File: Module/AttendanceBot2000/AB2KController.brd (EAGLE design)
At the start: 107.6 x 80 mm, 51 parts, among them IC1 74AHCT1G04DBV, IC2 74AHCT1G04DBV, IC3 LM386M-1, U1 L298, U2 QRE1113, U3 QRE1113, U4 QRE1113, U5 QRE1113, U6 QRE1113

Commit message: More progress on routing
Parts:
- added JP11: GO_LIGHT, SparkFun-Connectors:SCREWTERMINAL-5MM-2
- added Q1, Q2, Q3, Q4, Q5, Q6: 2N3904, transistor-npn:TO92
- added R11, R12, R13, R14, R15, R16: 1K, resistor:M1206
- moved JP4 37.5 mm to (39.4, 6.35), turned to 0 degrees
- moved JP9 29.5 mm to (38.1, 14.0)
- moved D1 24.7 mm to (33.0, 8.89)
- moved IC2 17.8 mm to (29.2, 24.1), turned to 270 degrees
- moved U$1 15.5 mm to (44.5, 35.6), turned to 180 degrees
- moved JP5 15.5 mm to (5.08, 20.3), turned to 270 degrees
- moved IC1 13.7 mm to (29.2, 17.8), turned to 270 degrees
- moved R7 10.8 mm to (81.3, 68.6), turned to 270 degrees
- moved JP10 7.18 mm to (52.1, 7.62), turned to 270 degrees
- moved R9 6.84 mm to (97.8, 63.5), turned to 270 degrees
- moved U1 5.08 mm to (20.3, 24.1)
- moved R10 2.54 mm to (88.9, 68.6)
- moved R8 2.54 mm to (71.1, 68.6)
- moved JP8 1.80 mm to (5.08, 48.3)
- moved JP6 1.27 mm to (5.08, 34.3)
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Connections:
- new net GO_IN: JP8.1, U$1.13
- new net GO_LT_ON: R16.2, U$1.12
- new net N$10: Q2.3, R3.2
- new net N$12: Q3.3, R5.2
- new net N$15: Q1.2, R11.1
- new net N$17: Q2.2, R12.1
- new net N$24: Q3.2, R13.1
- new net N$26: Q4.2, R14.1
- new net N$29: Q5.2, R15.1
- new net N$30: Q4.3, R7.2
- new net N$31: Q5.3, R9.2
- new net N$6: JP11.1, Q6.1
- new net N$9: Q1.3, R1.2
- net GND: now also Q6.3
- net N$25: now also Q6.2, R16.1; no longer JP8.1, U$1.5
- net SEN_0: now also U$1.18; no longer U$1.17
- net SEN_1: now also U$1.17; no longer U$1.18
- net VCC: now also R11.2, R12.2, R13.2, R14.2, R15.2; no longer R1.2, R3.2, R5.2, R7.2, R9.2
- net V_IN: now also JP11.2, Q1.1, Q2.1, Q3.1, Q4.1, Q5.1
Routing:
- net V_IN: track 0.00 -> 148.9 mm, vias 0 -> 1
- net VCC: track 0.00 -> 133.5 mm
- net GND: track 39.4 -> 98.8 mm
- net N$3: track 0.00 -> 28.6 mm
- net N$2: track 0.00 -> 22.0 mm
- net SEN_0: track 20.7 -> 0.00 mm, vias 1 -> 0
- net SEN_2: track 0.00 -> 18.2 mm, vias 0 -> 1
- net N$14: track 0.00 -> 16.4 mm
- net SEN_3: track 0.00 -> 15.6 mm, vias 0 -> 1
- net SEN_4: track 0.00 -> 15.5 mm, vias 0 -> 1
- net N$1: track 0.00 -> 14.6 mm
- net N$4: track 0.00 -> 13.6 mm
- net N$13: track 0.00 -> 12.1 mm
- net N$11: track 0.00 -> 12.1 mm
- net N$9: track 0.00 -> 11.3 mm
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- added copper zone on layer 16, net GND
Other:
- board size 107.6 x 80 mm -> 101.3 x 80 mm

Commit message: More layout complete
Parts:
- removed C4, C5: 0.15, resistor:C1206K
- removed C6, C7: 10, resistor:D/7343-31W
- removed JP9: FTDI Basic Prog. Port, SparkFun-Connectors:1X06
- moved C2 78.3 mm to (38.1, 66.0), turned to 90 degrees
- moved R16 74.5 mm to (29.2, 50.8), turned to 90 degrees
- moved JP11 58.5 mm to (5.08, 48.3), turned to 270 degrees
- moved Q6 58.0 mm to (22.9, 49.5), turned to 270 degrees
- moved C1 56.9 mm to (63.5, 66.0), turned to 90 degrees
- moved JP10 39.4 mm to (62.2, 45.7), turned to 0 degrees
- moved C3 26.2 mm to (67.3, 11.4), turned to 90 degrees
- moved C10 25.0 mm to (86.4, 38.1), turned to 90 degrees
- moved C8 15.3 mm to (95.2, 25.4), turned to 90 degrees
- moved R22 14.0 mm to (85.1, 6.35)
- moved C9 13.7 mm to (94.0, 16.5), turned to 180 degrees
- moved R23 11.7 mm to (87.6, 12.7)
- moved IC3 11.4 mm to (87.6, 26.7)
- moved JP8 10.2 mm to (15.2, 48.3)
- moved R21 8.98 mm to (87.6, 16.5)
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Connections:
- removed net DTR: JP9.1, U$1.GRN
- net GND: no longer C4.2, C5.2, C6.-, C7.-, JP9.5, JP9.6, U$1.BLK, U$1.GND
- net RXD_TTL: no longer JP9.3, U$1.RXI
- net SEN_3: now also U$1.A6; no longer U$1.20
- net SEN_4: now also U$1.A7; no longer U$1.A4
- net TXD_TTL: no longer JP9.2, U$1.TXO
- net VCC: no longer C4.1, C5.1, C6.+, C7.+, JP9.4, U$1.VCC
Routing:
- net GND: track 98.8 -> 196.1 mm, vias 0 -> 3
- net SEN_0: track 0.00 -> 79.0 mm, vias 0 -> 1
- net SEN_4: track 15.5 -> 86.8 mm, vias 1 -> 2
- net V_IN: track 148.9 -> 212.7 mm, vias 1 -> 7
- net AUDIO_RESET: track 0.00 -> 55.9 mm, vias 0 -> 2
- net DIRB_H: track 0.00 -> 51.9 mm, vias 0 -> 1
- net SEN_3: track 15.6 -> 66.5 mm, vias 1 -> 2
- net VCC: track 133.5 -> 181.8 mm
- net N$27: track 0.00 -> 46.8 mm
- net SEN_1: track 15.7 -> 58.1 mm
- net DIRA_H: track 0.00 -> 38.6 mm
- net SEN_2: track 18.2 -> 55.4 mm
- net R_PWM: track 0.00 -> 33.5 mm
- net DIRB_L: track 0.00 -> 32.9 mm, vias 0 -> 1
- net AUD_TXD: track 0.00 -> 27.9 mm
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- removed copper zone on layer 16, net GND

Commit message: Finished routing.  Sleep on it for a day
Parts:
- removed FRAME2: FRAME-LETTER, SparkFun-Aesthetics:CREATIVE_COMMONS
- added JP9: SERIAL, SparkFun-Connectors:1X03
- JP3: value L_MOT -> SPKR
- moved JP3 26.7 mm to (66.0, 6.35)
- moved C3 2.54 mm to (67.3, 14.0)
- moved JP1 2.54 mm to (61.0, 38.1)
- moved JP2 2.54 mm to (81.3, 38.1)
- moved JP7 2.54 mm to (66.0, 29.2)
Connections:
- net GND: now also JP9.2
- net RXD_TTL: now also JP9.1
- net TXD_TTL: now also JP9.3
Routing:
- net L_PWM: track 0.00 -> 79.9 mm, vias 0 -> 1
- net GND: track 196.1 -> 250.9 mm, vias 3 -> 6
- net V_IN: track 212.7 -> 245.7 mm, vias 7 -> 8
- net N$19: track 27.3 -> 60.3 mm
- net RXD_TTL: track 0.00 -> 26.7 mm
- net DIRA_L: track 0.00 -> 15.7 mm, vias 0 -> 1
- net TXD_TTL: track 0.00 -> 14.0 mm
- net DIRA_H: track 38.6 -> 50.0 mm
- net DIRB_H: track 51.9 -> 60.8 mm, vias 1 -> 2
- net AUDIO_RESET: track 55.9 -> 61.0 mm
- net VCC: track 181.8 -> 184.3 mm, vias 0 -> 2
- net SEN_0: track 79.0 -> 76.5 mm
- net N$27: track 46.8 -> 49.4 mm
- net AUD_TXD: track 27.9 -> 25.4 mm
- net AUD_RXD: track 27.9 -> 25.4 mm
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- added copper zone on layer 16, net GND
- added copper zone on layer 1, net VCC
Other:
- board text added: "+ -"
- board text added: "AUDIO"
- board text added: "AttBot2K (C) M. H. Reilly"
- board text added: "LED"
- board text added: "PWR +"
- board text added: "RST"
- board text added: "SEL_SERIAL"
- board text added: "SPKR"
- board text added: "SW"
- board text added: "T G R"
- board text added: "TRAIN_ENA"
- board text added: "VIN"

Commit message: submitted board A0 to OSH Park
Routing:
- net GND: track 250.9 -> 245.8 mm
- net VCC: track 184.3 -> 182.4 mm
- net N$16: track 22.3 -> 23.4 mm
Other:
- board text added: "AttBot2K Rev A.0 (C) M. H. Reilly JAN 21 2016"
- board text removed: "AttBot2K (C) M. H. Reilly"

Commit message: Fixed mis-wiring of AUD_TXD and AUD_RXD in sch and board.
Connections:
- net AUD_RXD: now also JP1.7; no longer JP1.6
- net AUD_TXD: now also JP1.8; no longer JP1.7
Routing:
- net AUD_TXD: track 25.4 -> 27.9 mm
- net AUD_RXD: track 25.4 -> 27.9 mm
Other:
- board text added: "AttBot2K Rev B.0 (C) M. H. Reilly JAN 21 2016"
- board text removed: "AttBot2K Rev A.0 (C) M. H. Reilly JAN 21 2016"
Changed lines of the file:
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@@
 <grid distance="0.05" unitdist="inch" unit="inch" style="lines" multiple="1" display="yes" altdistance="0.005" altunitdist="inch" altunit="inch"/>
 <layers>
-<layer number="1" name="Top" color="4" fill="1" visible="no" active="yes"/>
+<layer number="1" name="Top" color="4" fill="1" visible="yes" active="yes"/>
 <layer number="2" name="Route2" color="1" fill="3" visible="no" active="no"/>
 <layer number="3" name="Route3" color="4" fill="3" visible="no" active="no"/>
@@
 <hole x="3.81" y="3.81" drill="3.2"/>
 <hole x="96.52" y="3.81" drill="3.2"/>
-<text x="6.35" y="2.54" size="1.778" layer="21">AttBot2K Rev A.0
+<text x="6.35" y="2.54" size="1.778" layer="21">AttBot2K Rev B.0
 (C) M. H. Reilly
 JAN 21 2016</text>
@@
 </signal>
 <signal name="AUD_TXD">
-<contactref element="JP1" pad="7"/>
 <contactref element="U$1" pad="8"/>
-<wire x1="60.96" y1="22.86" x2="57.15" y2="22.86" width="0.4064" layer="1"/>
-<wire x1="57.15" y1="22.86" x2="57.15" y2="40.64" width="0.4064" layer="1"/>
+<wire x1="57.15" y1="20.32" x2="57.15" y2="40.64" width="0.4064" layer="1"/>
 <wire x1="57.15" y1="40.64" x2="53.34" y2="40.64" width="0.4064" layer="1"/>
+<contactref element="JP1" pad="8"/>
+<wire x1="57.15" y1="20.32" x2="60.96" y2="20.32" width="0.4064" layer="1"/>
 </signal>
 <signal name="AUD_RXD">
-<contactref element="JP1" pad="6"/>
 <contactref element="U$1" pad="9"/>
 <wire x1="53.34" y1="43.18" x2="58.42" y2="43.18" width="0.4064" layer="1"/>
-<wire x1="58.42" y1="43.18" x2="58.42" y2="25.4" width="0.4064" layer="1"/>
-<wire x1="58.42" y1="25.4" x2="60.96" y2="25.4" width="0.4064" layer="1"/>
+<wire x1="58.42" y1="43.18" x2="58.42" y2="22.86" width="0.4064" layer="1"/>
+<contactref element="JP1" pad="7"/>
+<wire x1="58.42" y1="22.86" x2="60.96" y2="22.86" width="0.4064" layer="1"/>
 </signal>
 <signal name="N$28">

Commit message: Fixed misconnect for UG vs CS...
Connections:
- net N$28: now also JP1.6; no longer JP1.5
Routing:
- net N$28: track 5.08 -> 7.62 mm
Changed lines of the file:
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@@
 </signal>
 <signal name="N$28">
-<contactref element="JP1" pad="5"/>
 <contactref element="JP7" pad="1"/>
-<wire x1="66.04" y1="27.94" x2="60.96" y2="27.94" width="0.4064" layer="16"/>
+<contactref element="JP1" pad="6"/>
+<wire x1="60.96" y1="25.4" x2="66.04" y2="25.4" width="0.4064" layer="1"/>
+<wire x1="66.04" y1="25.4" x2="66.04" y2="27.94" width="0.4064" layer="1"/>
 </signal>
 <signal name="GO_IN">

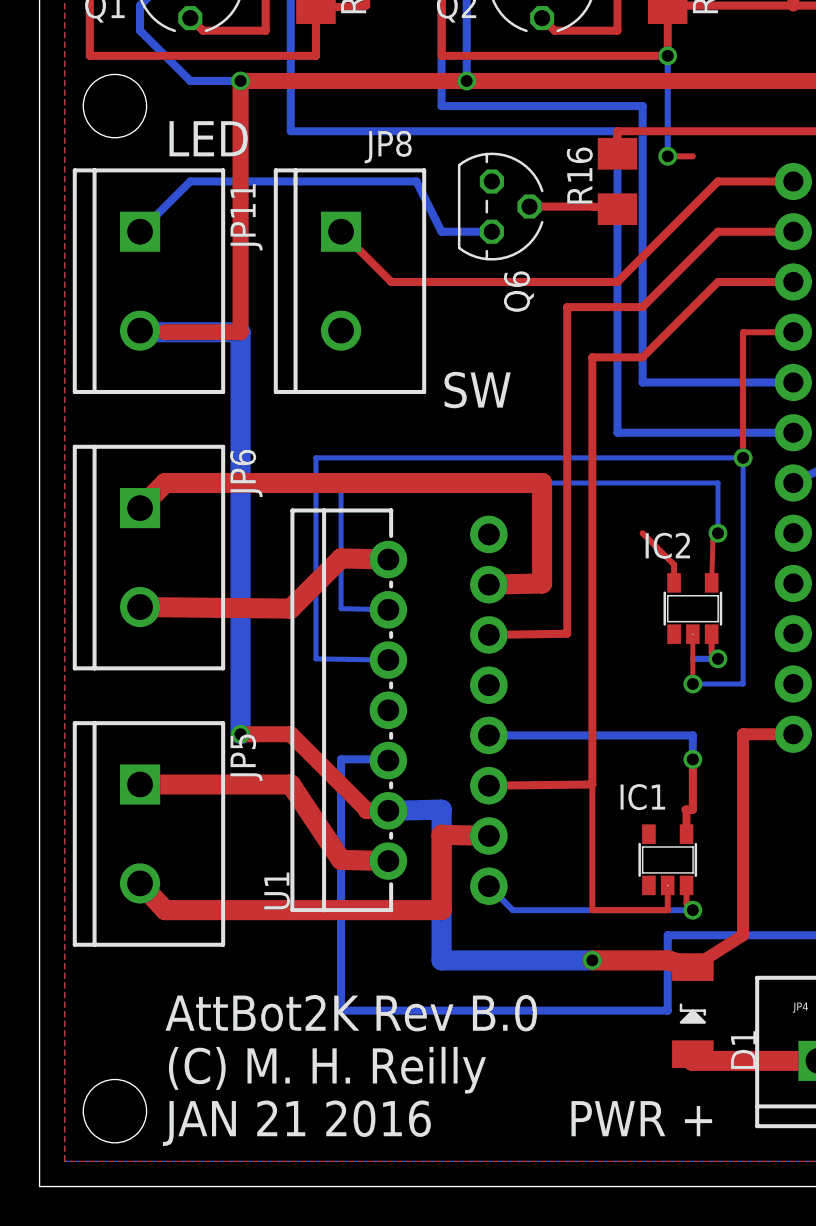
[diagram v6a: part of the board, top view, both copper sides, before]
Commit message: Added snubber diodes to motor outputs.
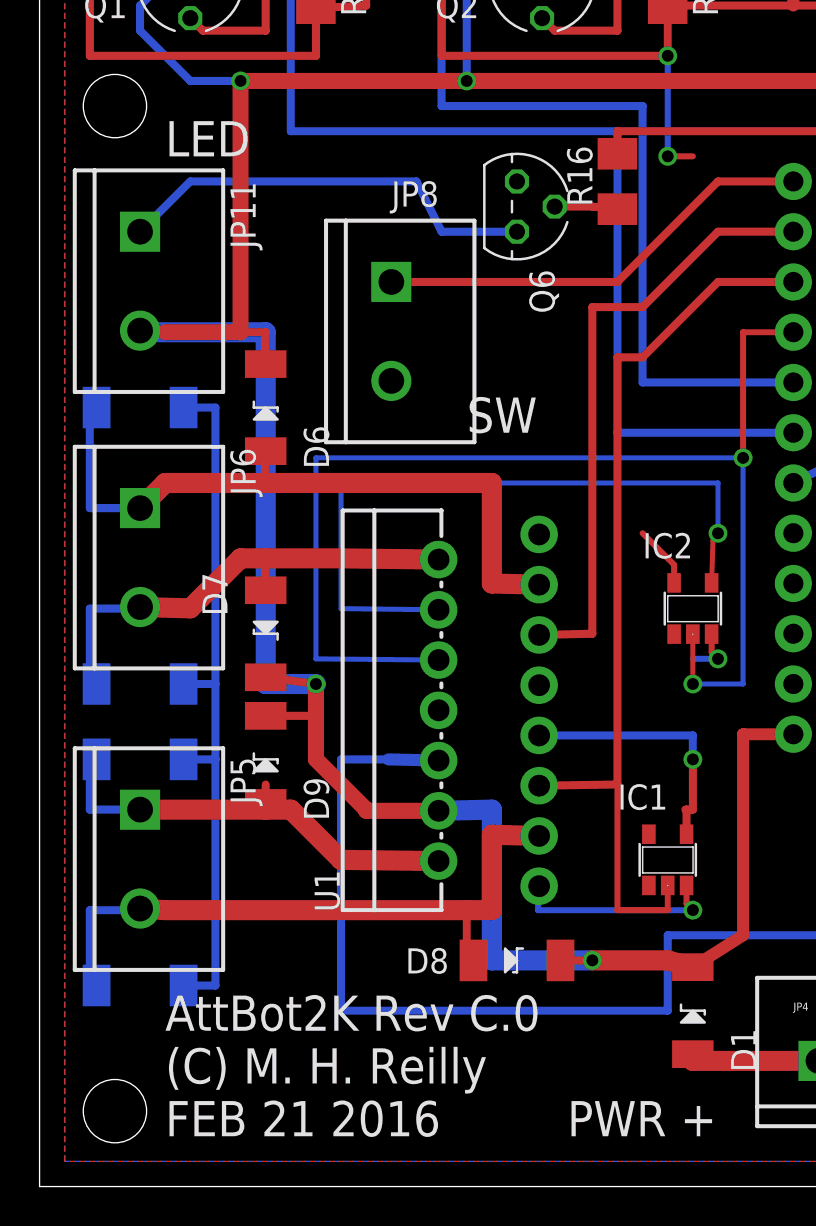
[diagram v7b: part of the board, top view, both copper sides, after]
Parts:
- added D2, D3, D4, D5, D6, D7, D8, D9: PMEG3030EP, kb1vc_robot_parts:SOD128
- moved JP8 3.59 mm to (17.8, 45.7)
- moved U1 2.54 mm to (22.9, 24.1)
- moved JP5 1.27 mm to (5.08, 19.1)
- moved Q6 1.27 mm to (24.1, 49.5)
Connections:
- net GND: now also D2.P$1, D3.P$1, D4.P$1, D5.P$1
- net N$1: now also D5.P$2, D9.P$1
- net N$2: now also D4.P$2, D8.P$1
- net N$3: now also D2.P$2, D6.P$1
- net N$4: now also D3.P$2, D7.P$1
- net V_IN: now also D6.P$2, D7.P$2, D8.P$2, D9.P$2
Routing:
- net GND: track 245.8 -> 279.7 mm
- net N$2: track 22.0 -> 33.6 mm
- net N$4: track 13.6 -> 24.5 mm
- net V_IN: track 245.7 -> 256.4 mm
- net N$1: track 14.6 -> 22.8 mm
- net N$3: track 28.6 -> 35.3 mm
- net DIRA_H: track 50.0 -> 46.2 mm
- net GO_IN: track 26.0 -> 22.4 mm
- net DIRA_L: track 15.7 -> 13.1 mm
- net DIRB_H: track 60.8 -> 63.3 mm
- net R_PWM: track 33.5 -> 30.9 mm
- net DIRB_L: track 32.9 -> 35.5 mm
- net L_PWM: track 79.9 -> 82.4 mm
- net N$6: track 20.4 -> 21.7 mm
- net N$25: track 4.45 -> 3.18 mm
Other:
- board text added: "AttBot2K Rev C.0 (C) M. H. Reilly FEB 21 2016"
- board text removed: "AttBot2K Rev B.0 (C) M. H. Reilly JAN 21 2016"
